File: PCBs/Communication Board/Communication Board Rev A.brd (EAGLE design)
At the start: 95.9 x 90.2 mm, 21 parts

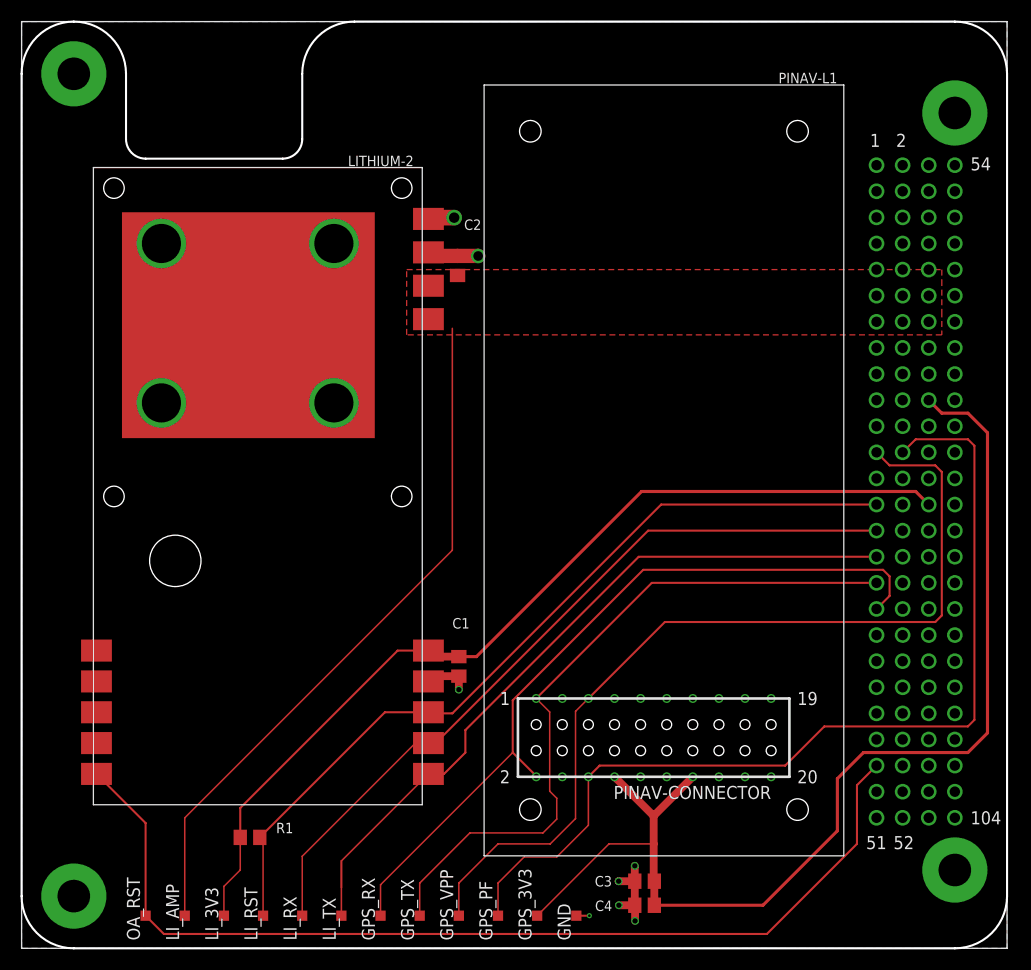
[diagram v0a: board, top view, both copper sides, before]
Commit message: Thermally couple radio to chassis
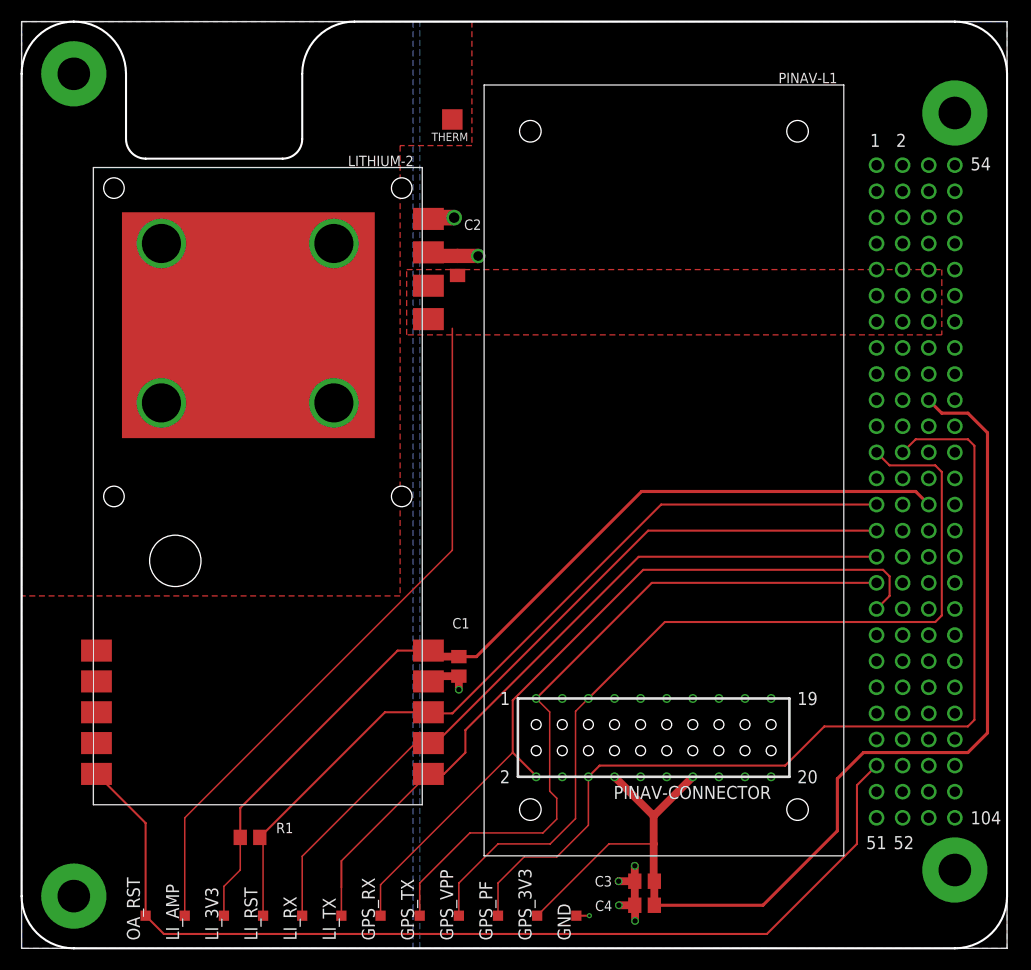
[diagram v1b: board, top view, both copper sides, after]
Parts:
- added THERM: TPSQTP20SQ, testpad:TP20SQ
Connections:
- new net MNT1: LITHIUM-2.RF_GND, LITHIUM-2.THERM1, LITHIUM-2.THERM2, LITHIUM-2.THERM3, LITHIUM-2.THERM4, THERM.TP, U$1.MNT1
- net GND: now also LITHIUM-2.GND; no longer LITHIUM-2.GND2, LITHIUM-2.RF_GND, LITHIUM-2.THERM1, LITHIUM-2.THERM2, LITHIUM-2.THERM3, LITHIUM-2.THERM4
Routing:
- added copper zone on layer 1, net MNT1
- added copper zone on layer 16, net MNT1
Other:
- board text added: "VT VCC Communication Board Rev A - 8/02/18"
- board text removed: "VT VCC Communications Board Rev A - 8/02/18"
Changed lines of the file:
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@@
 <wire x1="27.305" y1="85.09" x2="32.385" y2="90.17" width="0.2032" layer="20" curve="-90"/>
 <wire x1="32.385" y1="90.17" x2="90.805" y2="90.17" width="0.2032" layer="20"/>
-<text x="80.645" y="88.9" size="1.778" layer="48" rot="R180">VT VCC Communications Board
+<text x="80.645" y="88.9" size="1.778" layer="48" rot="R180">VT VCC Communication Board
 Rev A - 8/02/18</text>
 <rectangle x1="33.569275" y1="80.686275" x2="33.581975" y2="80.692625" layer="200"/>
@@
 <attribute name="VALUE" x="24.765" y="9.8298" size="1.016" layer="27"/>
 </element>
+<element name="THERM" library="testpad" library_urn="urn:adsk.eagle:library:385" package="TP20SQ" package3d_urn="urn:adsk.eagle:package:27980/1" value="TPSQTP20SQ" x="41.91" y="80.645" smashed="yes">
+<attribute name="NAME" x="39.894" y="78.5454" size="0.8128" layer="25"/>
+<attribute name="TP_SIGNAL_NAME" value="" x="41.91" y="78.105" size="1" layer="37"/>
+</element>
 </elements>
 <signals>
@@
 <contactref element="C1" pad="2"/>
 <contactref element="C2" pad="2"/>
-<polygon width="0.2032" layer="16">
-<vertex x="0" y="90.17"/>
+<polygon width="0.2032" layer="16" rank="2">
+<vertex x="38.735" y="90.17"/>
 <vertex x="95.885" y="90.17"/>
 <vertex x="95.885" y="0"/>
-<vertex x="0" y="0"/>
+<vertex x="38.735" y="0"/>
 </polygon>
 <contactref element="C4" pad="2"/>
@@
 <wire x1="53.975" y1="3.175" x2="55.245" y2="3.175" width="0.2032" layer="1"/>
 <via x="55.245" y="3.175" extent="1-16" drill="0.254"/>
-<contactref element="LITHIUM-2" pad="THERM3"/>
-<contactref element="LITHIUM-2" pad="THERM1"/>
-<contactref element="LITHIUM-2" pad="THERM2"/>
-<contactref element="LITHIUM-2" pad="THERM4"/>
-<contactref element="LITHIUM-2" pad="GND2"/>
+<contactref element="LITHIUM-2" pad="GND"/>
 <contactref element="LITHIUM-2" pad="RF_GND1"/>
 <contactref element="LITHIUM-2" pad="RF_GND2"/>
-<contactref element="LITHIUM-2" pad="RF_GND"/>
 <wire x1="39.585" y1="70.97" x2="39.7096" y2="71.0946" width="1.524" layer="1"/>
 <wire x1="39.7096" y1="71.0946" x2="42.0878" y2="71.0946" width="1.524" layer="1"/>
@@
 <wire x1="39.585" y1="67.371" x2="42.418" y2="67.371" width="1.397" layer="1"/>
 <wire x1="42.418" y1="67.371" x2="44.4144" y2="67.371" width="1.397" layer="1"/>
-<wire x1="30.385" y1="53.07" x2="22.065" y2="60.63" width="0" layer="19" extent="1-1"/>
 <wire x1="44.4144" y1="67.371" x2="44.4246" y2="67.3608" width="1.397" layer="1"/>
 </signal>
@@
 <wire x1="39.37" y1="22.97" x2="35.35" y2="22.97" width="0.2032" layer="1"/>
 </signal>
+<signal name="MNT1">
+<contactref element="LITHIUM-2" pad="THERM4"/>
+<contactref element="LITHIUM-2" pad="THERM1"/>
+<contactref element="LITHIUM-2" pad="RF_GND"/>
+<contactref element="LITHIUM-2" pad="THERM2"/>
+<contactref element="LITHIUM-2" pad="THERM3"/>
+<polygon width="0.1524" layer="1" thermals="no">
+<vertex x="0" y="90.17"/>
+<vertex x="10.16" y="90.17"/>
+<vertex x="43.815" y="90.17"/>
+<vertex x="43.815" y="78.105"/>
+<vertex x="36.83" y="78.105"/>
+<vertex x="36.83" y="34.29"/>
+<vertex x="0" y="34.29"/>
+</polygon>
+<polygon width="0.1524" layer="16" thermals="no">
+<vertex x="0" y="90.17"/>
+<vertex x="10.16" y="90.17"/>
+<vertex x="38.1" y="90.17"/>
+<vertex x="38.1" y="76.2"/>
+<vertex x="38.1" y="0"/>
+<vertex x="0" y="0"/>
+</polygon>
+<contactref element="THERM" pad="TP"/>
+<contactref element="U$1" pad="MNT1"/>
+</signal>
 </signals>

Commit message: Pass DRC
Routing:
- net 3V3: track 92.5 -> 91.9 mm
- net GND: track 22.5 -> 22.0 mm
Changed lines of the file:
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@@
 <wire x1="27.305" y1="85.09" x2="32.385" y2="90.17" width="0.2032" layer="20" curve="-90"/>
 <wire x1="32.385" y1="90.17" x2="90.805" y2="90.17" width="0.2032" layer="20"/>
-<text x="80.645" y="88.9" size="1.778" layer="48" rot="R180">VT VCC Communication Board
+<text x="79.375" y="89.535" size="1.778" layer="48" rot="R180">VT VCC Communication Board
 Rev A - 8/02/18</text>
 <rectangle x1="33.569275" y1="80.686275" x2="33.581975" y2="80.692625" layer="200"/>
@@
 <contactref element="LITHIUM-2" pad="RF_GND1"/>
 <contactref element="LITHIUM-2" pad="RF_GND2"/>
-<wire x1="39.585" y1="70.97" x2="39.7096" y2="71.0946" width="1.524" layer="1"/>
-<wire x1="39.7096" y1="71.0946" x2="42.0878" y2="71.0946" width="1.524" layer="1"/>
 <via x="42.0878" y="71.0946" extent="1-16" drill="1.016"/>
-<wire x1="39.585" y1="25.97" x2="39.52" y2="26.035" width="0.762" layer="1"/>
-<wire x1="40.037" y1="67.72" x2="39.585" y2="67.72" width="1.524" layer="1"/>
 <via x="44.4246" y="67.3608" extent="1-16" drill="0.9398"/>
 <wire x1="42.545" y1="26.482" x2="40.097" y2="26.482" width="0.762" layer="1"/>
@@
 <wire x1="42.418" y1="67.371" x2="44.4144" y2="67.371" width="1.397" layer="1"/>
 <wire x1="44.4144" y1="67.371" x2="44.4246" y2="67.3608" width="1.397" layer="1"/>
+<wire x1="42.0878" y1="71.0946" x2="39.7096" y2="71.0946" width="1.524" layer="1"/>
+<wire x1="39.7096" y1="71.0946" x2="39.585" y2="70.97" width="1.524" layer="1"/>
 </signal>
 <signal name="GPS_TX">
@@
 <wire x1="86.995" y1="44.45" x2="88.265" y2="43.18" width="0.3048" layer="1"/>
 <contactref element="LITHIUM-2" pad="3.3V"/>
-<wire x1="40.018" y1="29.403" x2="39.585" y2="28.97" width="0.762" layer="1"/>
 <wire x1="39.585" y1="28.97" x2="36.59" y2="28.97" width="0.2032" layer="1"/>
 <wire x1="42.545" y1="28.382" x2="40.173" y2="28.382" width="0.762" layer="1"/>
@@
 <mfgpreviewcolor name="substratecolor" color="0xFF786E46"/>
 </mfgpreviewcolors>
+<errors>
+</errors>
 </board>
 </drawing>
